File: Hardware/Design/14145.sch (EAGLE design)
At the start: 103 parts, among them J1 B, J2 RJ45J, J3 PBC10SAAN, J4 RJ45J, J5 PBC10SAAN, J6 PBC10SAAN, J7 PBC08SAAN, J8 PPPC032LFBN, Q1 DMB, Q2 K38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

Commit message: Hardware: ^4 review
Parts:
- removed C13: 0.1uF, C-C:CC0603A
- removed D1: SQ4, D-SBR:DSMA
- removed R19: 200k, R-C:R0805
- removed R20: 10k, R-C:R0805
- added TP13, TP14, TP8: TPPAD1-08, J-TP:TPPAD1-08
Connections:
- removed net VIN: D1.K, J7.1, R19.1, U5.EN, U5.IN
- removed net VIN_ADC7: C13.1, R19.2, R20.1, U7.(A7/T3/MOSI1)PE3
- new net N$1: TP8.TP, U7.(ICP1)PB0
- net +5V: now also U5.EN, U5.IN; no longer D1.A, R11.1
- net 0V: no longer C13.2, R20.2
- net DTR_RXD: now also TP14.TP; no longer U7.(ICP1)PB0
- net DTR_TXD: now also TP13.TP
- net IOREF: now also R11.1
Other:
- note added: "1/14/17"
- note added: "ICP1 TO TP"
- note added: "^4"
- note removed: "4.98mV/V"

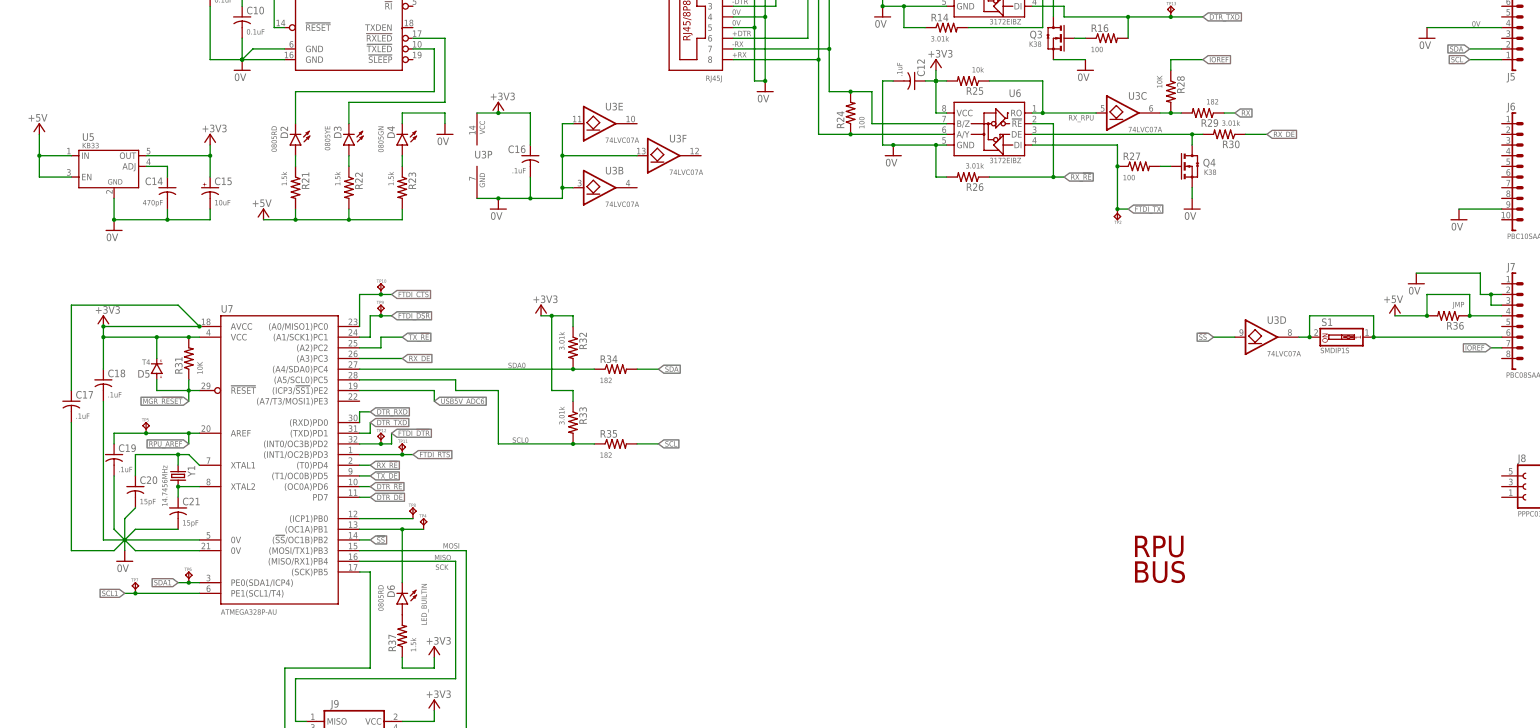
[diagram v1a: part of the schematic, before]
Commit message: Hardware: arrange parts and their references
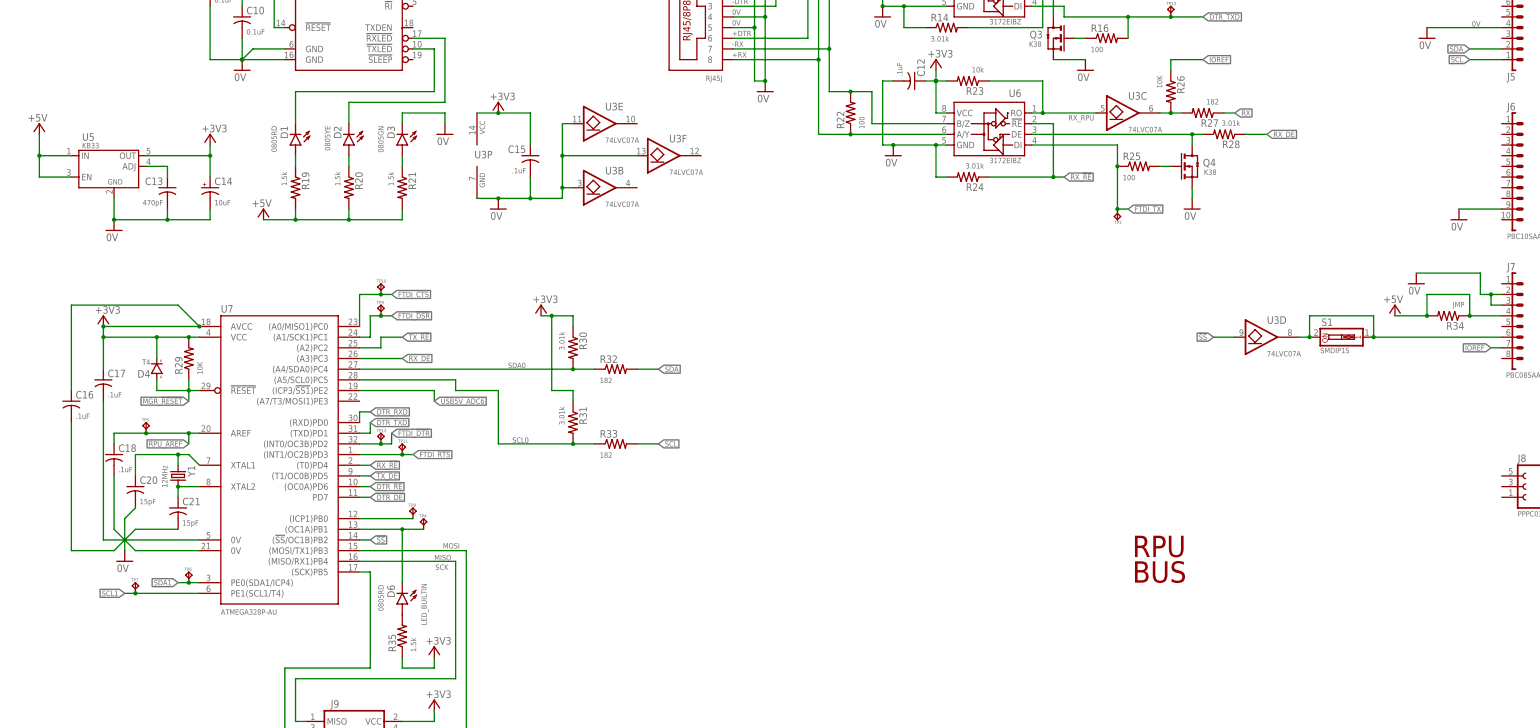
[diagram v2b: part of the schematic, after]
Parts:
- removed C19: .1uF, C-C:CC0603A
- removed D5: T4, D-GP:DSOD123
- removed R36: JMP, R-C:R0805
- removed R37: 1.5k, R-C:R0805
- added C13: 470pF, C-C:CC0603A
- added D1: 0805RD, D-LED:LEDC0805(2012)
- added R19, R20: 1.5k, R-C:R0805
- C14: value 470pF -> 10uF; device C-C:CC0603A -> C-T:CT1206
- C15: value 10uF -> .1uF; device C-T:CT1206 -> C-C:CC0603A
- D2: value 0805RD -> 0805YE
- D3: value 0805YE -> 0805GN
- D4: value 0805GN -> T4; device D-LED:LEDC0805(2012) -> D-GP:DSOD123
- R22: value 1.5k -> 100
- R23: value 1.5k -> 10k
- R24: value 100 -> 3.01k
- R25: value 10k -> 100
- R26: value 3.01k -> 10K
- R27: value 100 -> 182
- R28, R31: value 10K -> 3.01k
- R29: value 182 -> 10K
- R32, R33: value 3.01k -> 182
- R34: value 182 -> JMP
- R35: value 182 -> 1.5k
- Y1: value 14.7456MHz -> 12MHz
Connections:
- net +3V3: now also C14.+, C15.1, D4.K, R23.2, R29.2, R30.1, R31.1, R35.1; no longer C15.+, C18.1, D5.K, R25.2, R31.2, R32.1, R33.1, R37.1
- net +5V: now also R19.2, R20.2, R34.1, R34.2; no longer R22.2, R23.2, R36.1, R36.2
- net +RX: now also R22.1; no longer R24.1
- net -RX: now also R22.2; no longer R24.2
- net 0V: now also C13.2, C14.-, C15.2, D3.K, R24.2; no longer C14.2, C15.-, C19.2, D4.K, R26.2
- net FTDI_TX: now also R25.1; no longer R27.1
- net IOREF: now also R26.1; no longer R28.1
- net MGR_!RESET: now also D4.A, R29.1; no longer D5.A, R31.1
- net N$10: now also R26.2, R27.2; no longer R28.2, R29.2
- net N$11: now also R28.2; no longer R30.2
- net N$14: now also D3.A, R21.1; no longer D4.A, R23.1
- net N$16: now also D1.A, R19.1; no longer D2.A, R21.1
- net N$24: now also C13.1; no longer C14.1
- net N$25: now also R25.2; no longer R27.2
- net N$29: now also R35.2; no longer R37.2
- net N$6: now also D2.A, R20.1; no longer D3.A, R22.1
- net N$7: now also D1.K; no longer D2.K
- net N$8: now also D2.K; no longer D3.K
- net RPU_AREF: now also C18.1; no longer C19.1
- net RX: now also R27.1; no longer R29.1
- net RX_!RE: now also R24.1; no longer R26.1
- net RX_DE: now also R28.1; no longer R30.1
- net RX_RPU: now also R23.1; no longer R25.1
- net SCL: now also R33.2; no longer R35.2
- net SCL0: now also R31.2, R33.1; no longer R33.2, R35.1
- net SDA: now also R32.2; no longer R34.2
- net SDA0: now also R30.2, R32.1; no longer R32.2, R34.1
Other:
- note added: "CRYSTAL NOT USED: ECS-120-20-3X-TR 12MHZ +/- 30PPM STABILITY AND TOLERANCE CRYSTAL CAPACITORS: 15PF = 5PF + (20PF*20PF)/(20PF+20PF)"
- note removed: "CRYSTAL NOT USED: ECS-147.4-20-3X-TR 14.7456MHZ +/- 30PPM STABILITY AND TOLERANCE CRYSTAL CAPACITORS: 15PF = 5PF + (20PF*20PF)/(20PF+20PF)"
- moved on the sheet: C16, C17, C18, D2, D3, R21, R22, R23, R24, R25, R26, R27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
